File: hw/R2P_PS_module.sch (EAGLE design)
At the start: 67 parts, among them U1 STM32F103CX, U4 TPS5450, U5 LD3985XX, X2 OSC-XTAL212M_

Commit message: Added R2 value
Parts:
- R2: value (none) -> 4k7
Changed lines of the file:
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@@
 <?xml version="1.0" encoding="utf-8"?>
 <!DOCTYPE eagle SYSTEM "eagle.dtd">
-<eagle version="6.2">
+<eagle version="6.4">
 <drawing>
 <settings>
@@
 <part name="D2" library="dp_devices" deviceset="ZENER" device="SOD-323F"/>
 <part name="GND8" library="supply" deviceset="GND" device=""/>
-<part name="R2" library="rcl" deviceset="R-EU_" device="R0603"/>
+<part name="R2" library="rcl" deviceset="R-EU_" device="R0603" value="4k7"/>
 <part name="Q1" library="transistor-power" deviceset="N-MOSFET-SO8" device="S"/>
 <part name="U4" library="DCDC" deviceset="TPS5450" device=""/>

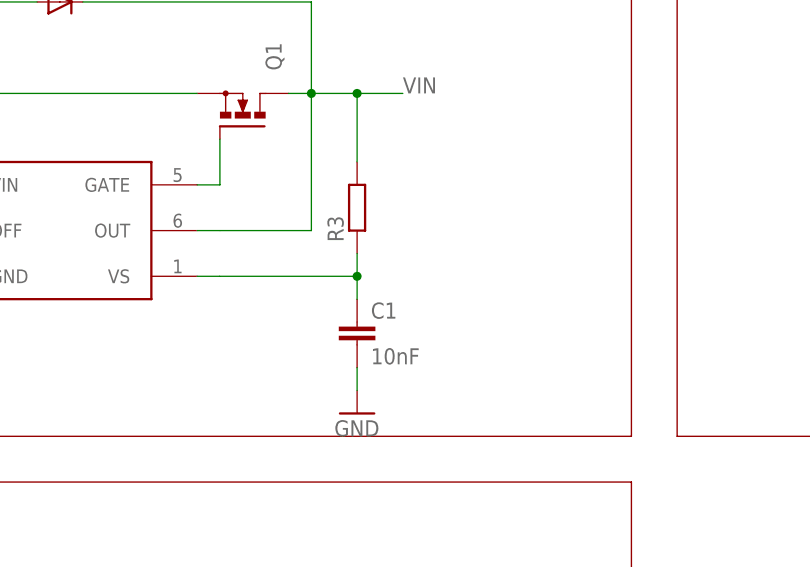
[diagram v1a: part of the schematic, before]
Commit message: added missing component values
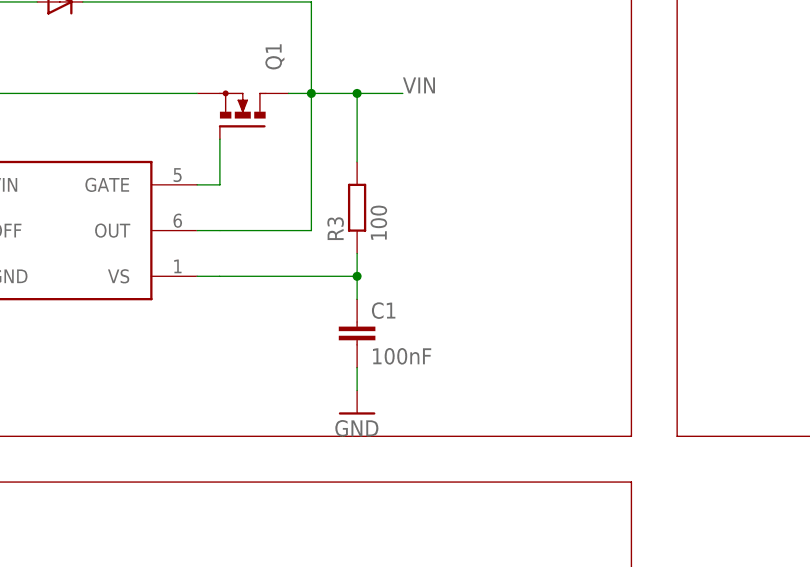
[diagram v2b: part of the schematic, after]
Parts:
- C1: value 10nF -> 100nF
- R3: value (none) -> 100
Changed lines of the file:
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@@
 <part name="D4" library="dp_devices" deviceset="ZENER" device="SOD-323F"/>
 <part name="GND41" library="supply" deviceset="GND" device=""/>
-<part name="R3" library="rcl" deviceset="R-EU_" device="R0603"/>
-<part name="C1" library="rcl" deviceset="C-EU" device="C0603" value="10nF"/>
+<part name="R3" library="rcl" deviceset="R-EU_" device="R0603" value="100"/>
+<part name="C1" library="rcl" deviceset="C-EU" device="C0603" value="100nF"/>
 <part name="GND9" library="supply" deviceset="GND" device=""/>
 <part name="C8" library="rcl" deviceset="CPOL-EU" device="E5-10.5"/>
